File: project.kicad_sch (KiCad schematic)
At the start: 31 parts, among them J1 7S_CSE_IAS, J10 LED_CPT_FD, J11 LED_AT, J12 NPS_BANK_ANGLE, J13 KD_N1, J14 KD_SPD, J15 KD_LVL_CHG, J16 KD_VNAV, J17 KD_HDG_SEL, J18 KD_APP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

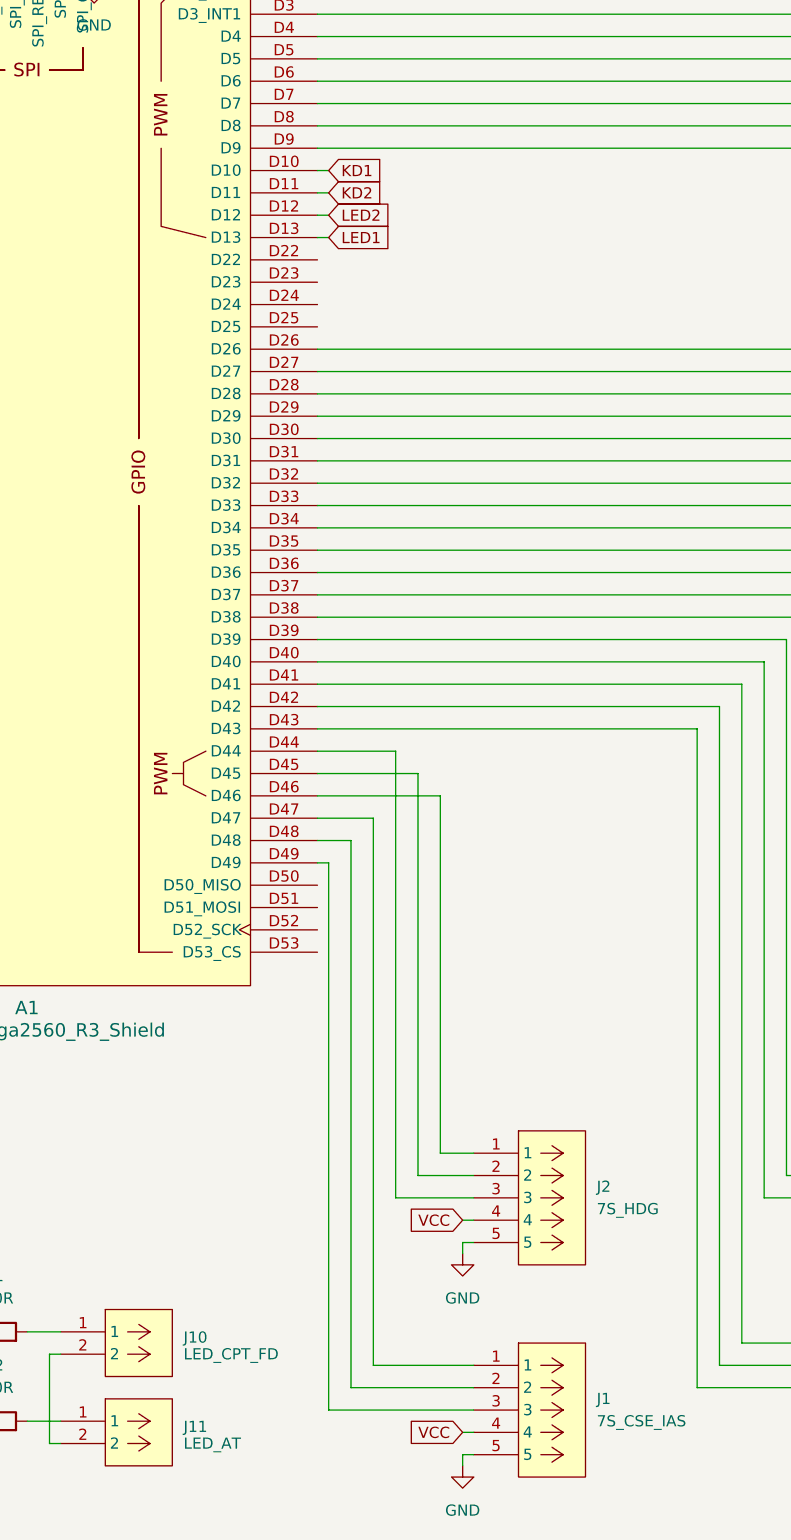
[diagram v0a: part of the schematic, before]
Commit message: feat: route south part of bottom layer
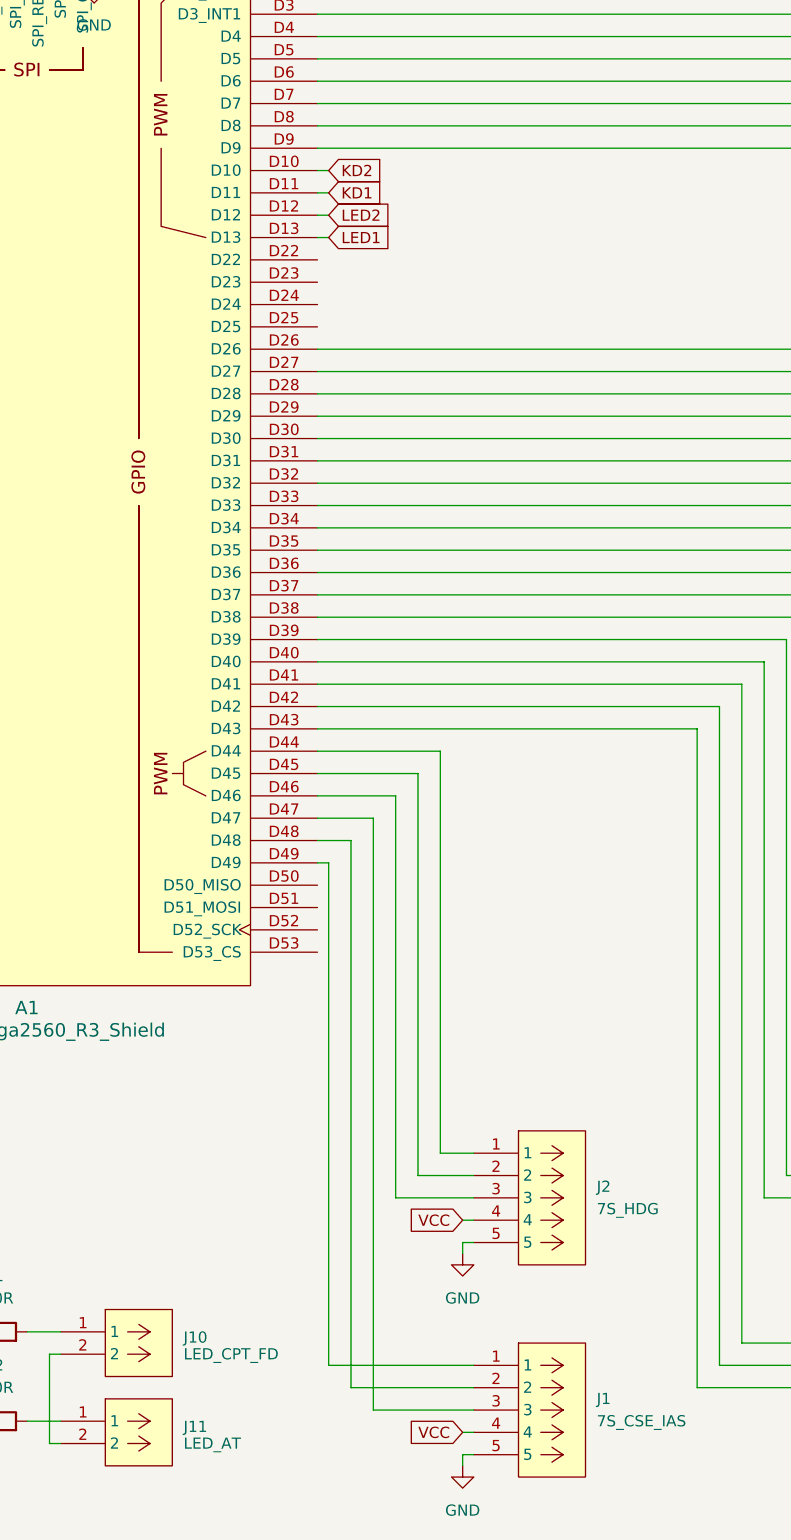
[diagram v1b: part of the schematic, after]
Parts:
- R1, R10, R2, R3, R4, R5, R6, R7, R8, R9: footprint (none) -> footprint_library:xs resistor PT; symbol Device:R -> symbol_library:R
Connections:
- net KD1: now also A1.D11; no longer A1.D10
- net KD2: now also A1.D10; no longer A1.D11
- net at J1.1: now also A1.D49; no longer A1.D47
- net at J1.3: now also A1.D47; no longer A1.D49
- net at A1.D44: now also J2.1; no longer J2.3
- net at A1.D46: now also J2.3; no longer J2.1
